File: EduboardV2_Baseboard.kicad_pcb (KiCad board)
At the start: 2 copper layers, 2 parts, among them IC301 XL1509-5.0E1, X201 PCIE-52P40H

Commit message: added more components
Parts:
- added B201: CR2032-BS-6-1, eduboardv2:BAT-TH_CR2032-BS-6-1, F.Cu at (213.4, 35.6)
- added BUZZER401: MLT-8530, eduboardv2:BUZ-SMD_4P-L8.5-W8.5-P8.50-TL, F.Cu at (139.1, 80.2)
- added C201: 10pF, eduboardv2:C0402, F.Cu at (256.0, 27.9)
- added C202: 1uF, eduboardv2:C0402, F.Cu at (215.3, 45.3)
- added C203: 10nF, eduboardv2:C0402, F.Cu at (208.6, 49.6)
- added C204: 100nF, eduboardv2:C0402, F.Cu at (208.6, 51.8)
- added C301: 220uF, 35V, eduboardv2:CAP-SMD_BD8.0-L8.3-W8.3-RD, F.Cu at (136.5, 109.1)
- added C302: 100nF, 50V, eduboardv2:C0402, F.Cu at (135.7, 122.2)
- added C303: 22pF, eduboardv2:C0402, F.Cu at (169.0, 94.8)
- added C304: 22pF, eduboardv2:C0402, F.Cu at (151.2, 109.8)
- added C305: 100nF, 50V, eduboardv2:C0402, F.Cu at (157.0, 106.2)
- added C306: 100nF, 50V, eduboardv2:C0402, F.Cu at (147.8, 115.2)
- added C307: 10uF, X5R, 25V, eduboardv2:C0603, F.Cu at (157.3, 103.8)
- added C308: 22pF, eduboardv2:C0402, F.Cu at (162.2, 100.5)
- added C309: 220uF, 35V, eduboardv2:CAP-SMD_BD8.0-L8.3-W8.3-RD, F.Cu at (124.9, 117.7)
- added C310: 10uF, X5R, 25V, eduboardv2:C0603, F.Cu at (164.5, 98.1)
- added C311: 100nF, 50V, eduboardv2:C0402, F.Cu at (143.8, 112.5)
- added C312: 1uF, 25V, eduboardv2:C0402, F.Cu at (132.2, 122.2)
- added C313: 10uF, X5R, 25V, eduboardv2:C0603, F.Cu at (148.1, 112.8)
- added C314: 100nF, 50V, eduboardv2:C0402, F.Cu at (144.9, 119.0)
- added C315: 1uF, 25V, eduboardv2:C0402, F.Cu at (151.9, 112.0)
- added C316: 220uF, 35V, eduboardv2:CAP-SMD_BD8.0-L8.3-W8.3-RD, F.Cu at (138.6, 98.6)
- added C401: 1nF, eduboardv2:C0402, F.Cu at (182.4, 52.3)
- added C402: 10nF, eduboardv2:C0402, F.Cu at (178.7, 56.6)
- added C403: 1nF, eduboardv2:C0402, F.Cu at (149.0, 63.7)
- added C404: 10nF, eduboardv2:C0402, F.Cu at (178.9, 54.5)
- added C405: 1nF, eduboardv2:C0402, F.Cu at (149.0, 61.5)
- added C406: 10nF, eduboardv2:C0402, F.Cu at (165.9, 67.0)
- added C407: 100nF, eduboardv2:C0402, F.Cu at (174.0, 59.5)
- added C408: 10nF, eduboardv2:C0402, F.Cu at (165.9, 69.2)
- added C409: 100nF, eduboardv2:C0402, F.Cu at (178.9, 52.3)
- added C410: 1uF, eduboardv2:C0402, F.Cu at (135.5, 89.6)
- added C411: 1uF, eduboardv2:C0402, F.Cu at (171.6, 64.0)
- added C601: 100nF, eduboardv2:C0402, F.Cu at (229.4, 61.5)
- added C602: 100nF, eduboardv2:C0402, F.Cu at (205.4, 80.6)
- added C603: 10uF, eduboardv2:C0603, F.Cu at (206.0, 78.2)
- added C604: 100nF, eduboardv2:C0402, F.Cu at (208.8, 80.6)
- added C605: 10uF, eduboardv2:C0603, F.Cu at (206.0, 73.4)
- added C606: 4.7uF, eduboardv2:C0603, F.Cu at (201.6, 80.0)
- added C607: 4.7uF, eduboardv2:C0603, F.Cu at (210.1, 73.4)
- added C608: 2.2nF, eduboardv2:C0402, F.Cu at (224.3, 67.8)
- added C609: 2.2nF, eduboardv2:C0402, F.Cu at (233.7, 59.8)
- added D201: B5819W_C8598, eduboardv2:SOD-123_L2.7-W1.6-LS3.7-RD-1, F.Cu at (250.4, 38.7)
- added D202: B5819W_C8598, eduboardv2:SOD-123_L2.7-W1.6-LS3.7-RD-1, F.Cu at (206.2, 47.0)
- added D301: SS210, eduboardv2:SMA_L4.3-W2.6-LS5.2-RD, F.Cu at (158.7, 95.8)
- added D302: SS210, eduboardv2:SMA_L4.3-W2.6-LS5.2-RD, F.Cu at (142.4, 115.9)
- added D303: SS210, eduboardv2:SMA_L4.3-W2.6-LS5.2-RD, F.Cu at (145.8, 109.4)
- added D304: SS210, eduboardv2:SMA_L4.3-W2.6-LS5.2-RD, F.Cu at (145.8, 105.4)
- added D305: blue, eduboardv2:LED0603-R-RD_BLUE, F.Cu at (164.9, 95.3)
- added D401: blue, eduboardv2:LED0603-R-RD_BLUE, F.Cu at (167.5, 64.5)
- added D402: blue, eduboardv2:LED0603-R-RD_BLUE, F.Cu at (161.8, 67.2)
- added D403: blue, eduboardv2:LED0603-R-RD_BLUE, F.Cu at (136.2, 87.0)
- added D404: blue, eduboardv2:LED0603-R-RD_BLUE, F.Cu at (174.7, 52.7)
- added D405: blue, eduboardv2:LED0603-R-RD_BLUE, F.Cu at (131.4, 88.2)
- added D406: blue, eduboardv2:LED0603-R-RD_BLUE, F.Cu at (126.6, 88.2)
- added D407: blue, eduboardv2:LED0603-R-RD_BLUE, F.Cu at (157.0, 67.2)
- added D408: blue, eduboardv2:LED0603-R-RD_BLUE, F.Cu at (121.7, 88.2)
- added D409: RGB-LED, eduboardv2:LED-SMD_FM-B2020RGBA-HG, F.Cu at (154.2, 79.2)
- added D410: WS2812B-B_W, eduboardv2:LED-SMD_4P-L5.0-W5.0-TL_WS2812B-B, F.Cu at (148.1, 80.7)
- added D411: 1N4148WST4, eduboardv2:SOD-323_L1.8-W1.3-LS2.5-RD, F.Cu at (156.7, 74.2)
- added IC201: STK8321, eduboardv2:LGA-12_L2.0-W2.0-P0.50-TR, F.Cu at (205.1, 50.8)
- added IC202: PCF8563T_5,518, eduboardv2:SOIC-8_L5.0-W4.0-P1.27-LS6.0-BL, F.Cu at (200.2, 48.4)
- added IC203: W25Q128JVSIQTR, eduboardv2:SOIC-8_L5.3-W5.3-P1.27-LS8.0-BL, F.Cu at (251.1, 32.0)
- added IC302: SY8113BADC, eduboardv2:TSOT-23-6_L2.9-W1.6-P0.95-LS2.8-BR, F.Cu at (140.8, 120.0)
- added IC601: STK8321, eduboardv2:LGA-12_L2.0-W2.0-P0.50-TR, F.Cu at (209.8, 77.0)
- added IC602: SP3485EN-L_TR, eduboardv2:SOIC-8_L5.0-W4.0-P1.27-LS6.0-BL, F.Cu at (196.4, 76.2)
- added IC603: WM8782SEDS_RV_C323842, eduboardv2:SSOP-20_L7.5-W5.2-P0.65-LS8.0-BL, F.Cu at (218.3, 71.7)
- added IC604: CS4344-CZZ, eduboardv2:TSSOP-10_L3.0-W3.0-P0.50-LS4.9-BL, F.Cu at (201.9, 75.3)
- added IC605: MCP9700AT-E_TT, eduboardv2:SOT-23-3_L2.9-W1.3-P1.90-LS2.4-BR, F.Cu at (229.8, 58.3)
- added L301: 6.8uH, 1A, eduboardv2:IND-SMD_L4.0-W4.0, F.Cu at (152.4, 106.1)
- added L302: 68uH, 1A, eduboardv2:IND-SMD_L6.0-W6.0_FNR60XXS, F.Cu at (134.6, 117.5)
- added L601: GZ1608D601TF, eduboardv2:L0603, F.Cu at (234.0, 57.5)
- added R301: 5.1k, eduboardv2:R0402, F.Cu at (168.0, 97.8)
- added R302: 5.1k, eduboardv2:R0402, F.Cu at (160.9, 103.6)
- added R303: 100k, eduboardv2:R0402, F.Cu at (154.5, 109.8)
- added R304: 22k, eduboardv2:R0402, F.Cu at (165.5, 100.5)
- added R305: 100k, eduboardv2:R0402, F.Cu at (151.6, 114.1)
- added R306: 1k, eduboardv2:R0402, F.Cu at (160.9, 105.7)
- added R401: 1k, eduboardv2:R0402, F.Cu at (153.6, 86.2)
- added R402: 10k, eduboardv2:R0402, F.Cu at (163.5, 76.1)
- added R403: 1k, eduboardv2:R0402, F.Cu at (169.2, 67.0)
- added R404: 50k, eduboardv2:RES-TH_RK09K1130AAU, F.Cu at (158.0, 60.9)
- added R405: 1k, eduboardv2:R0402, F.Cu at (150.8, 88.4)
- added R406: 1k, eduboardv2:R0402, F.Cu at (144.8, 89.1)
- added R407: 1k, eduboardv2:R0402, F.Cu at (157.4, 78.8)
- added R408: 1k, eduboardv2:R0402, F.Cu at (174.9, 63.8)
- added R409: 10k, eduboardv2:R0402, F.Cu at (163.4, 74.0)
- added R410: 1k, eduboardv2:R0402, F.Cu at (172.2, 68.3)
- added R411: 50k, eduboardv2:RES-TH_RK09K1130AAU, F.Cu at (126.3, 70.1)
- added R412: 1k, eduboardv2:R0402, F.Cu at (185.6, 52.3)
- added R413: 1k, eduboardv2:R0402, F.Cu at (160.5, 78.3)
- added R414: 1k, eduboardv2:R0402, F.Cu at (169.2, 69.2)
- added R415: 50k, eduboardv2:RES-TH_RK09K1130AAU, F.Cu at (140.3, 70.1)
- added R416: 1k, eduboardv2:R0402, F.Cu at (173.8, 61.7)
- added R417: 10k, eduboardv2:R0402, F.Cu at (147.8, 89.1)
- added R418: 150R, eduboardv2:R0402, F.Cu at (160.4, 74.0)
- added R419: 150R, eduboardv2:R0402, F.Cu at (156.6, 83.0)
- added R420: 1k, eduboardv2:R0402, F.Cu at (168.3, 71.3)
- added R421: 10k, eduboardv2:R0402, F.Cu at (180.3, 58.8)
- added R422: 150R, eduboardv2:R0402, F.Cu at (157.4, 76.6)
- added R423: 10R, eduboardv2:R0402, F.Cu at (153.3, 81.9)
- added R424: 10R, eduboardv2:R0402, F.Cu at (153.6, 84.1)
- added R425: 10R, eduboardv2:R0402, F.Cu at (176.8, 61.7)
- added R426: 10R, eduboardv2:R0402, F.Cu at (177.3, 59.5)
- added R427: 10R, eduboardv2:R0402, F.Cu at (165.3, 71.3)
- added R428: 10R, eduboardv2:R0402, F.Cu at (157.4, 80.9)
- added R429: NP, eduboardv2:R0402, F.Cu at (185.2, 54.5)
- added R430: 10R, eduboardv2:R0402, F.Cu at (160.5, 76.1)
- added R431: NP, eduboardv2:R0402, F.Cu at (172.2, 66.2)
- added R432: 10R, eduboardv2:R0402, F.Cu at (166.5, 73.5)
- added R433: 10R, eduboardv2:R0402, F.Cu at (150.5, 84.9)
- added R434: NP, eduboardv2:R0402, F.Cu at (181.9, 56.6)
- added R435: 10R, eduboardv2:R0402, F.Cu at (182.1, 54.5)
- added R601: 10k, eduboardv2:R0402, F.Cu at (215.1, 80.0)
- added R602: 120R, eduboardv2:R0402, F.Cu at (232.7, 61.9)
- added R603: 10k, eduboardv2:R0402, F.Cu at (227.6, 67.8)
- added R604: 10k, eduboardv2:R0402, F.Cu at (212.1, 79.8)
- added R605: 10k, eduboardv2:R0402, F.Cu at (215.1, 77.9)
- added R606: 470R, eduboardv2:R0402, F.Cu at (229.2, 63.6)
- added R607: 470R, eduboardv2:R0402, F.Cu at (224.1, 70.0)
- added SW401: K2-1102SP-C4SC-04, eduboardv2:KEY-SMD_4P-L6.0-W6.0-P4.50-LS9.5-BL, F.Cu at (150.9, 71.6)
- added SW402: K2-1102SP-C4SC-04, eduboardv2:KEY-SMD_4P-L6.0-W6.0-P4.50-LS9.5-BL, F.Cu at (130.2, 80.8)
- added SW403: K2-1102SP-C4SC-04, eduboardv2:KEY-SMD_4P-L6.0-W6.0-P4.50-LS9.5-BL, F.Cu at (122.9, 80.8)
- added SW404: K2-1102SP-C4SC-04, eduboardv2:KEY-SMD_4P-L6.0-W6.0-P4.50-LS9.5-BL, F.Cu at (168.7, 57.1)
- added T401: AO3400A, eduboardv2:SOT-23-3_L2.9-W1.6-P1.90-LS2.8-BR, F.Cu at (161.4, 70.8)
- added T402: AO3400A, eduboardv2:SOT-23-3_L2.9-W1.6-P1.90-LS2.8-BR, F.Cu at (174.6, 56.3)
- added T403: AO3400A, eduboardv2:SOT-23-3_L2.9-W1.6-P1.90-LS2.8-BR, F.Cu at (140.9, 87.7)
- added T404: AO3400A, eduboardv2:SOT-23-3_L2.9-W1.6-P1.90-LS2.8-BR, F.Cu at (146.7, 85.9)
- added T405: AO3400A, eduboardv2:SOT-23-3_L2.9-W1.6-P1.90-LS2.8-BR, F.Cu at (156.8, 70.8)
- added X202: 32.768 kHz, eduboardv2:FC-135R_L3.2-W1.5, F.Cu at (211.3, 45.6)
- added X203: TF-15×15, eduboardv2:TF-SMD_TF-15-15, F.Cu at (236.9, 36.2)
- added X301: KF2EDGR-3.81-3P, eduboardv2:CONN-TH_3P-P3.81_KF2EDGR-3.81-3P, F.Cu at (126.2, 95.7)
- added X302: USB3.1C16PFSMT, eduboardv2:USB-C-SMD_TYPE-C-USB-17, F.Cu at (149.6, 97.6)
- added X303: CH340G, eduboardv2:SOIC-16_L9.9-W3.9-P1.27-LS6.0-BL, F.Cu at (125.3, 108.5)
- added X401: ER-TFT035-6, eduboardv2:FPC-SMD_AFC07-S50ECA-00, F.Cu at (135.2, 53.6)
- added X501: PH-00650, eduboardv2:HDR-SMD_40P-P2.54-V-M-R2-C20-S7.8-EH, F.Cu at (145.5, 31.7)
- added X502: S4B-PH-SM4-K-TB(LF)(SN), eduboardv2:CONN-SMD_S4B-PH-SM4-K-TB-LF-SN, F.Cu at (126.2, 42.1)
- added X503: USB3.1C16PFSMT, eduboardv2:USB-C-SMD_TYPE-C-USB-17, F.Cu at (177.2, 30.7)
- added X601: KF2EDGR-3.81-3P, eduboardv2:CONN-TH_3P-P3.81_KF2EDGR-3.81-3P, F.Cu at (220.9, 58.1)
- added X602: PJ-327C-4A, eduboardv2:AUDIO-SMD_PJ-327C-4A, F.Cu at (197.9, 65.8)
- added X603: PJ-327C-4A, eduboardv2:AUDIO-SMD_PJ-327C-4A, F.Cu at (208.6, 65.8)
- added Y301: X322512MSB4SI, eduboardv2:OSC-SMD_4P-L3.2-W2.5-BL, F.Cu at (157.9, 100.0)
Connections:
- IC301 pad 1: unconnected-(IC301-Pad1) -> V_EXT
- IC301 pad 2: unconnected-(IC301-Pad2) -> Net-(IC301-Pad2)
- IC301 pad 3: unconnected-(IC301-Pad3) -> +5V_EXT
- IC301 pad 5: unconnected-(IC301-Pad5) -> GND
- IC301 pad 6: unconnected-(IC301-Pad6) -> GND
- IC301 pad 7: unconnected-(IC301-Pad7) -> GND
- IC301 pad 8: unconnected-(IC301-Pad8) -> GND

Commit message: fixed RTC Symbol
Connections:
- IC202 pad 1: (no net) -> Net-(C201-Pad1)

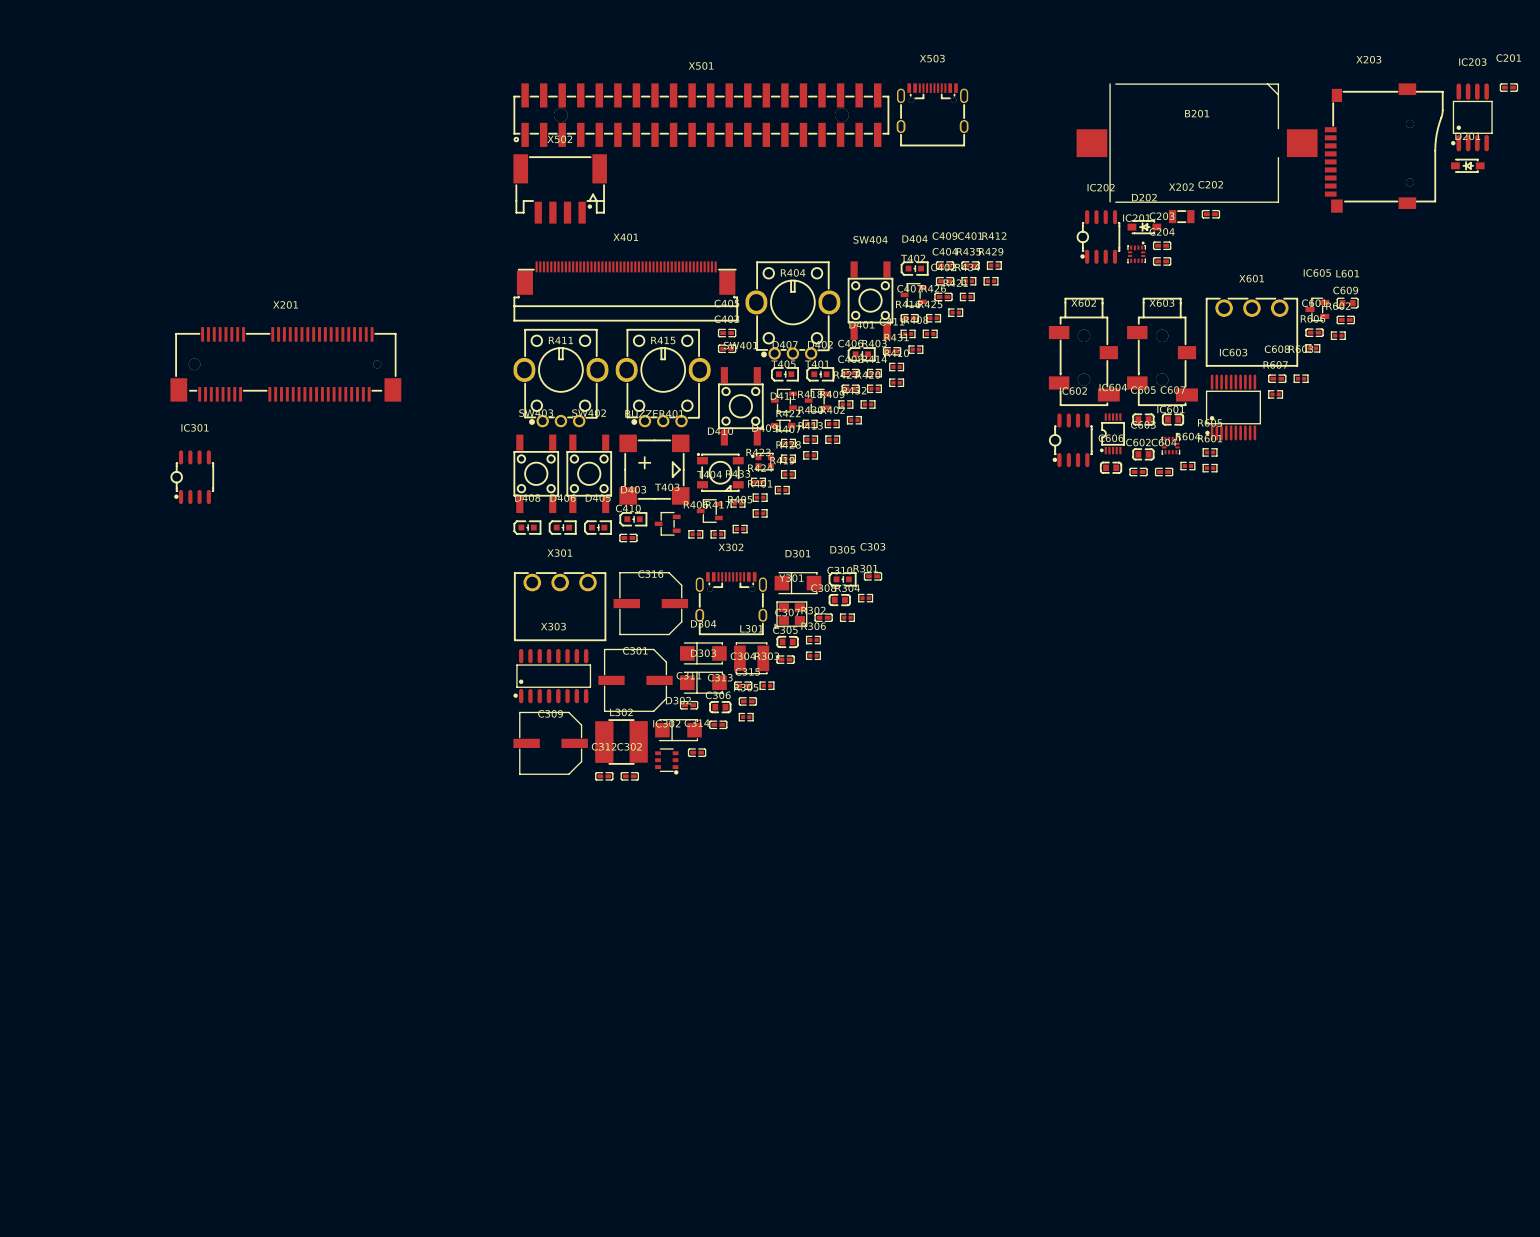
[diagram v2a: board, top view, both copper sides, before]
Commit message: Rough pcb placement for space estimation. Exchanged 40P connector
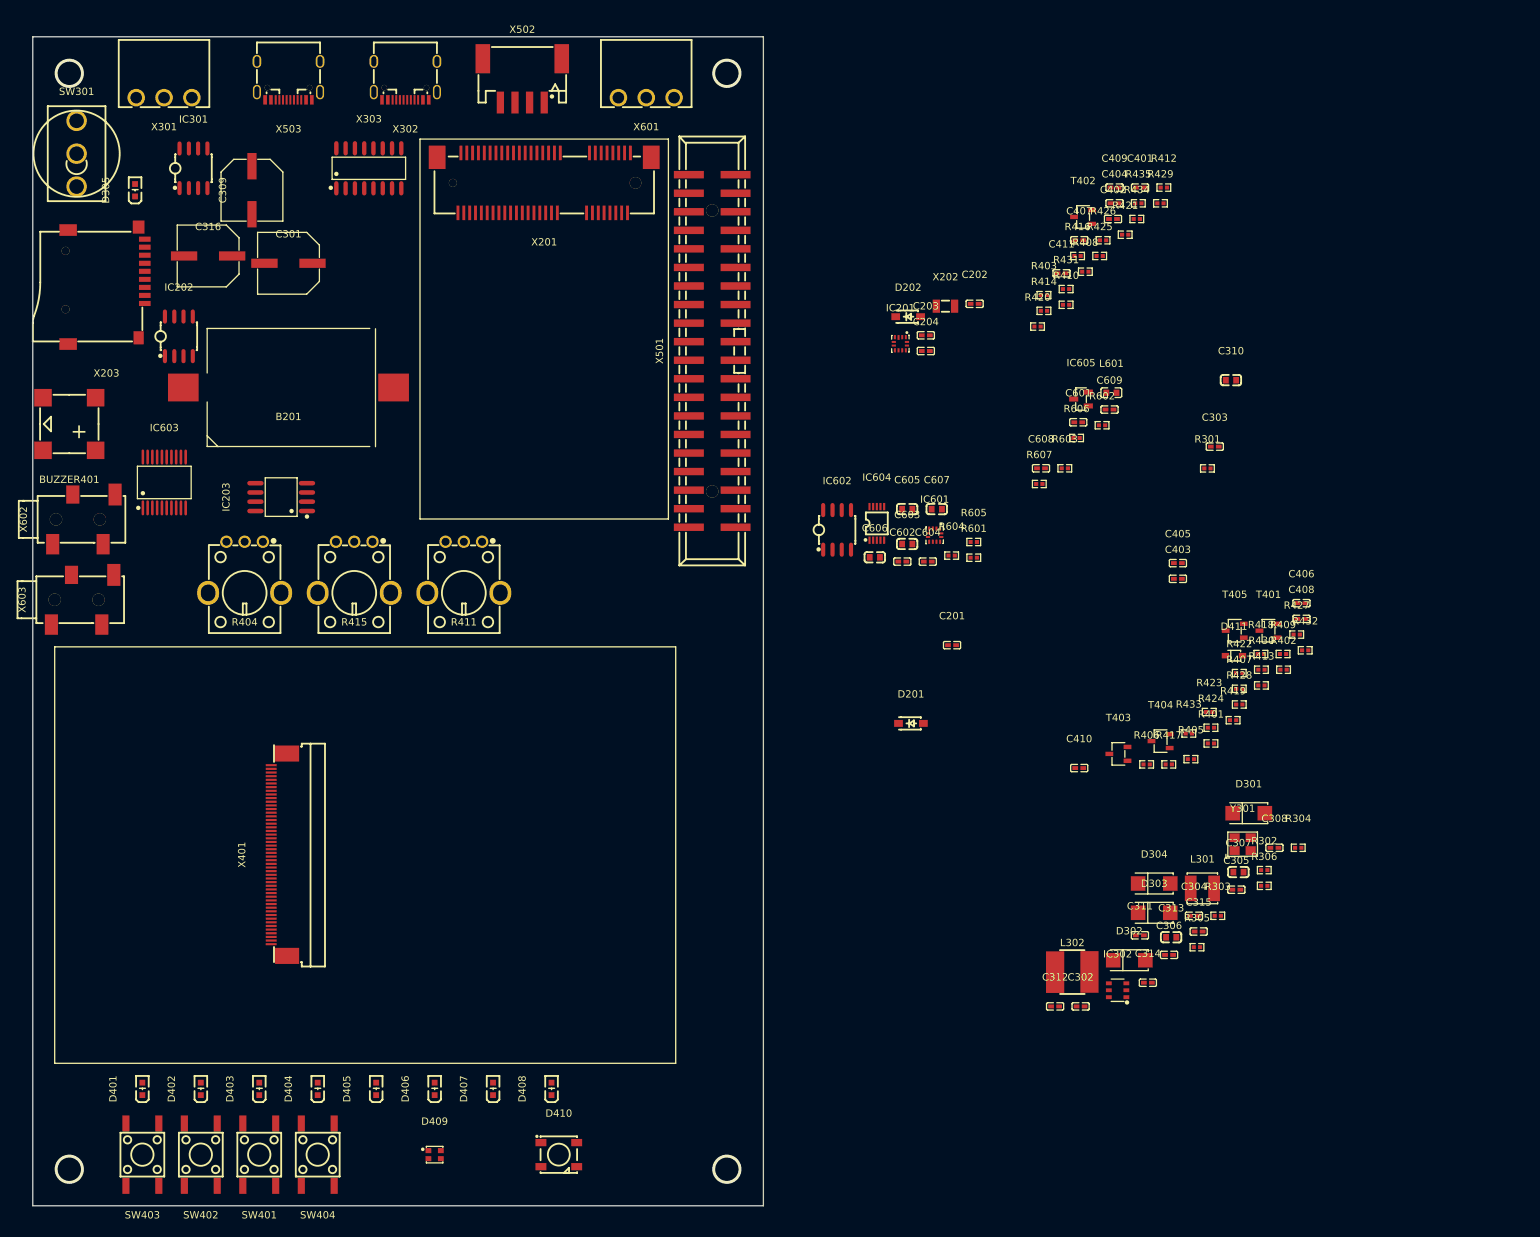
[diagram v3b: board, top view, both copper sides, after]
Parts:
- added SW301: 1FS1T1B9M2RES-5, eduboardv2:SW-TH_1FS1T1B9M2RES-5, F.Cu at (60.0, 37.0)
- X501: value PH-00650 -> BH-00105; footprint eduboardv2:HDR-SMD_40P-P2.54-V-M-R2-C20-S7.8-EH -> eduboardv2:IDC-SMD_BH-00105
- moved X203 173.8 mm to (64.1, 55.0), turned to 180 degrees
- moved IC203 171.2 mm to (88.0, 84.0), turned to 90 degrees
- moved X603 151.2 mm to (60.8, 98.0), turned to 90 degrees
- moved IC603 146.7 mm to (72.0, 82.0)
- moved D401 140.7 mm to (69.0, 165.0), turned to 90 degrees
- moved SW404 139.2 mm to (93.0, 174.0), turned to 180 degrees
- moved D404 138.9 mm to (93.0, 165.0), turned to 90 degrees
- moved X602 138.5 mm to (61.0, 87.0), turned to 90 degrees
- moved D402 129.5 mm to (77.0, 165.0), turned to 90 degrees
- moved B201 128.8 mm to (89.0, 69.0), turned to 180 degrees
- moved IC202 127.0 mm to (74.0, 62.0)
- moved SW401 121.8 mm to (85.0, 174.0), turned to 180 degrees
- moved D305 110.5 mm to (68.0, 42.0), turned to 90 degrees
- moved C201 107.9 mm to (179.8, 104.3)
- moved D201 107.9 mm to (174.2, 115.0)
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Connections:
- D302 pad 1: +5V -> Net-(D302-Pad1)
- D303 pad 1: +5V -> Net-(D302-Pad1)
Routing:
- net (no net): vias 0 -> 4
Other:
- board outline added: 100 x 160 mm
